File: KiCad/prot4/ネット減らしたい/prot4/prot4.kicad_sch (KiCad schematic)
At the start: 217 parts, among them J1 Conn_01x02_Socket, J2 LED_SW, J3 Conn_01x04_Socket, Q1 Q_Photo_NPN, Q10 Q_Photo_NPN, Q11 Q_Photo_NPN, Q12 Q_Photo_NPN, Q13 Q_Photo_NPN, Q14 Q_Photo_NPN, Q15 Q_Photo_NPN, Q16 Q_Photo_NPN, Q17 Q_Photo_NPN, Q18 Q_Photo_NPN, Q19 Q_Photo_NPN, Q2 Q_Photo_NPN, Q20 Q_Photo_NPN, Q21 Q_Photo_NPN, Q22 Q_Photo_NPN, Q23 Q_Photo_NPN, Q24 Q_Photo_NPN, Q25 Q_Photo_NPN, Q26 Q_Photo_NPN, Q27 Q_Photo_NPN, Q28 Q_Photo_NPN, Q29 Q_Photo_NPN, Q3 Q_Photo_NPN, Q30 Q_Photo_NPN, Q31 Q_Photo_NPN, Q32 Q_Photo_NPN, Q4 Q_Photo_NPN, Q5 Q_Photo_NPN, Q6 Q_Photo_NPN, Q7 Q_Photo_NPN, Q8 Q_Photo_NPN, Q9 Q_Photo_NPN, U1 LM393, U10 LM393, U11 LM393, U12 LM393, U13 LM393, U14 LM393, U15 LM393, U16 LM393, U2 LM393, U3 LM393, U4 LM393, U5 LM393, U6 LM393, U7 LM393, U8 LM393, U9 LM393

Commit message: 半球終了
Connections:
- net 1: now also RP2040_Zero1., RP2040_Zero1.8 (7)
- net 2: now also RP2040_Zero1.9 (8)
- net 21: now also RP2040_Zero1.17 (26)
- net 22: now also RP2040_Zero1.16 (15)
- net 23: now also RP2040_Zero1.15 (14)
- net 24: now also RP2040_Zero1.10 (9)
- net 25: now also RP2040_Zero1.4 (3)
- net 26: now also RP2040_Zero1.11 (10)
- net 27: now also RP2040_Zero1.14 (13)
- net 28: now also RP2040_Zero1.5 (4)
- net 29: now also RP2040_Zero1.12 (11)
- net 30: now also RP2040_Zero1.13 (12)
- net 31: now also RP2040_Zero1.6 (5)
- net 32: now also RP2040_Zero1.7 (6)
- net OUT_RX: now also RP2040_Zero1.20 (29); no longer RP2040_Zero1.14 (13)
- net OUT_TX: now also RP2040_Zero1.19 (28); no longer RP2040_Zero1.13 (12)
- net RP1_RX: now also RP2040_Zero2.19 (28); no longer RP2040_Zero2.5 (4)
- net RP1_TX: now also RP2040_Zero2.20 (29); no longer RP2040_Zero2.6 (5)

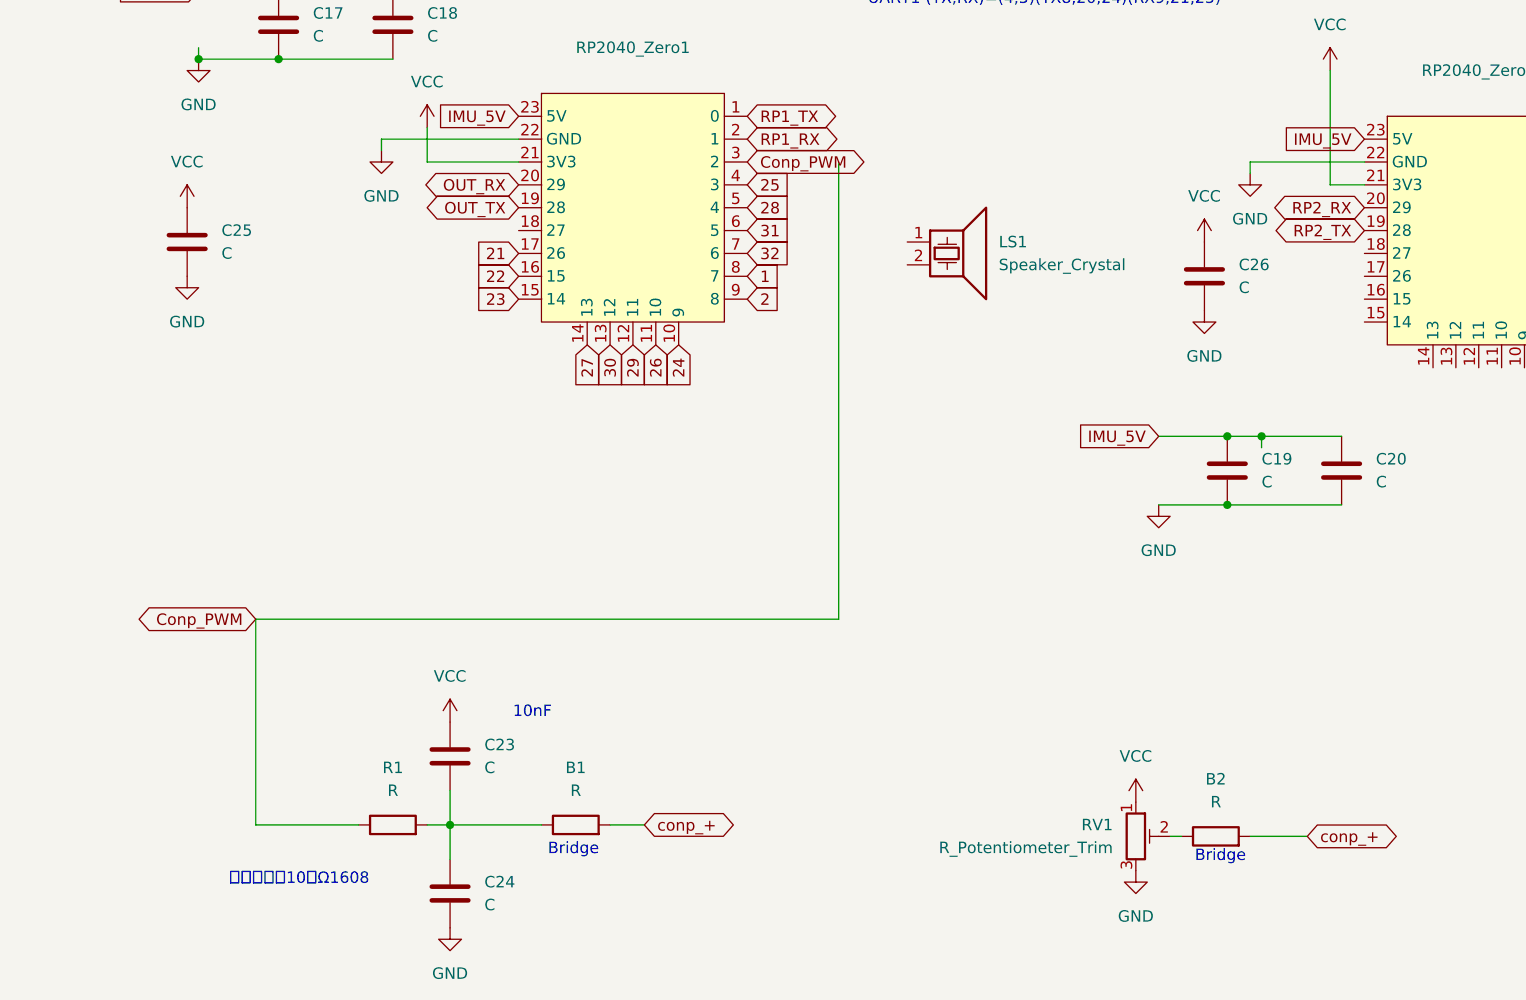
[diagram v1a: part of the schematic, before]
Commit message: 平滑化用コンデンサTHTにした、0.1uFと10kΩ？
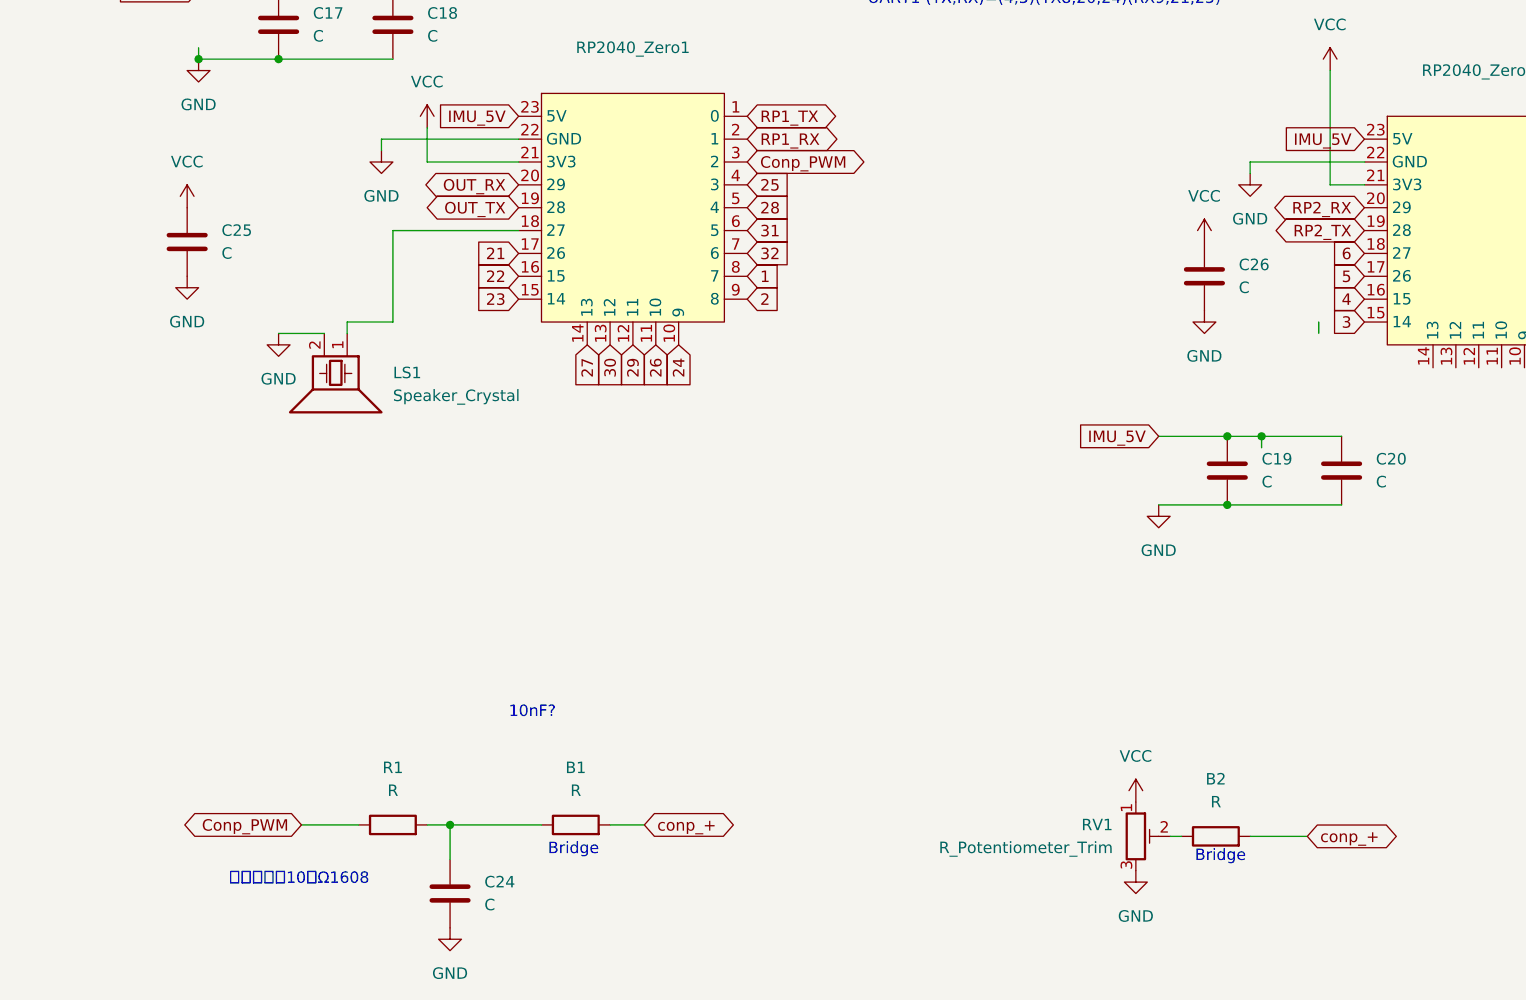
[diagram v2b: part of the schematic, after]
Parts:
- removed C23: C, Capacitor_SMD:C_0603_1608Metric_Pad1.08x0.95mm_HandSolder, symbol Device:C
- C24: footprint Capacitor_SMD:C_0603_1608Metric_Pad1.08x0.95mm_HandSolder -> Capacitor_THT:C_Rect_L7.0mm_W2.0mm_P5.00mm
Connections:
- net 3: now also RP2040_Zero2.15 (14)
- net 4: now also RP2040_Zero2.16 (15)
- net 5: now also RP2040_Zero2.17 (26)
- net 6: now also RP2040_Zero2.18 (27)
- net GND: now also LS1.2
- net at LS1.1: now also RP2040_Zero1.18 (27)
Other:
- note added: "10nF?"
- note removed: "10nF"
- moved on the sheet: LS1

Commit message: 配線終了
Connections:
- net 10: now also RP2040_Zero2.1 (0)
- net 11: now also RP2040_Zero2.12 (11)
- net 12: now also RP2040_Zero2.14 (13)
- net 13: now also RP2040_Zero2.13 (12)
- net 14: now also RP2040_Zero2.9 (8)
- net 15: now also RP2040_Zero2.5 (4)
- net 16: now also RP2040_Zero2., RP2040_Zero2.8 (7)
- net 17: now also RP2040_Zero2.4 (3)
- net 18: now also RP2040_Zero2.7 (6)
- net 19: now also RP2040_Zero2.3 (2)
- net 20: now also RP2040_Zero2.6 (5)
- net 7: now also RP2040_Zero2.10 (9)
- net 8: now also RP2040_Zero2.11 (10)
- net 9: now also RP2040_Zero2.2 (1)
